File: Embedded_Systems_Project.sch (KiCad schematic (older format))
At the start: 1 part

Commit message: Deleted the Mcu
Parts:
- removed U?: ATmega2560-16AU, Package_QFP:TQFP-100_14x14mm_P0.5mm, symbol MCU_Microchip_ATmega:ATmega2560-16AU
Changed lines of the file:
@@
 Comment4 ""
 $EndDescr
-$Comp
-L MCU_Microchip_ATmega:ATmega2560-16AU U?
-U 1 1 606B9968
-P 4750 3800
-F 0 "U?" H 4750 811 50  0000 C CNN
-F 1 "ATmega2560-16AU" H 4650 3850 50  0000 C CNN
-F 2 "Package_QFP:TQFP-100_14x14mm_P0.5mm" H 4750 3800 50  0001 C CIN
-F 3 "http://ww1.microchip.com/downloads/en/DeviceDoc/Atmel-2549-8-bit-AVR-Microcontroller-ATmega640-1280-1281-2560-2561_datasheet.pdf" H 4750 3800 50  0001 C CNN
-	1    4750 3800
-	1    0    0    -1
-$EndComp
 $EndSCHEMATC

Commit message: updated component schematic
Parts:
- added U?: ATmega2560, symbol ATmega2560:ATmega2560
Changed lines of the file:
@@
 encoding utf-8
 Sheet 1 1
-Title "ESP"
+Title "Embedded Systems Projects"
 Date "2021-04-05"
 Rev "v1.0"
-Comp "studnts"
+Comp "students"
 Comment1 "firs trial"
 Comment2 ""
@@
 Comment4 ""
 $EndDescr
+$Comp
+L ATmega2560:ATmega2560 U?
+U 1 1 606C76A0
+P 5200 3750
+F 0 "U?" H 6744 3921 50  0000 L CNN
+F 1 "ATmega2560" H 6744 3830 50  0000 L CNN
+F 2 "" H 3100 6850 50  0001 C CNN
+F 3 "" H 3100 6850 50  0001 C CNN
+	1    5200 3750
+	1    0    0    -1
+$EndComp
 $EndSCHEMATC

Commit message: added footprint
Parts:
- U1: renamed from U?; footprint (none) -> Package_QFP:TQFP-100_14x14mm_P0.5mm
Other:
- moved on the sheet: U1
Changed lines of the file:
@@
 $EndDescr
 $Comp
-L ATmega2560:ATmega2560 U?
+L ATmega2560:ATmega2560 U1
 U 1 1 606C76A0
-P 5200 3750
-F 0 "U?" H 6744 3921 50  0000 L CNN
-F 1 "ATmega2560" H 6744 3830 50  0000 L CNN
-F 2 "" H 3100 6850 50  0001 C CNN
-F 3 "" H 3100 6850 50  0001 C CNN
-	1    5200 3750
+P 7800 3200
+F 0 "U1" H 9344 3371 50  0000 L CNN
+F 1 "ATmega2560" H 9344 3280 50  0000 L CNN
+F 2 "Package_QFP:TQFP-100_14x14mm_P0.5mm" H 5700 6300 50  0001 C CNN
+F 3 "https://ww1.microchip.com/downloads/en/DeviceDoc/ATmega640-1280-1281-2560-2561-Datasheet-DS40002211A.pdf" H 5700 6300 50  0001 C CNN
+	1    7800 3200
 	1    0    0    -1
 $EndComp

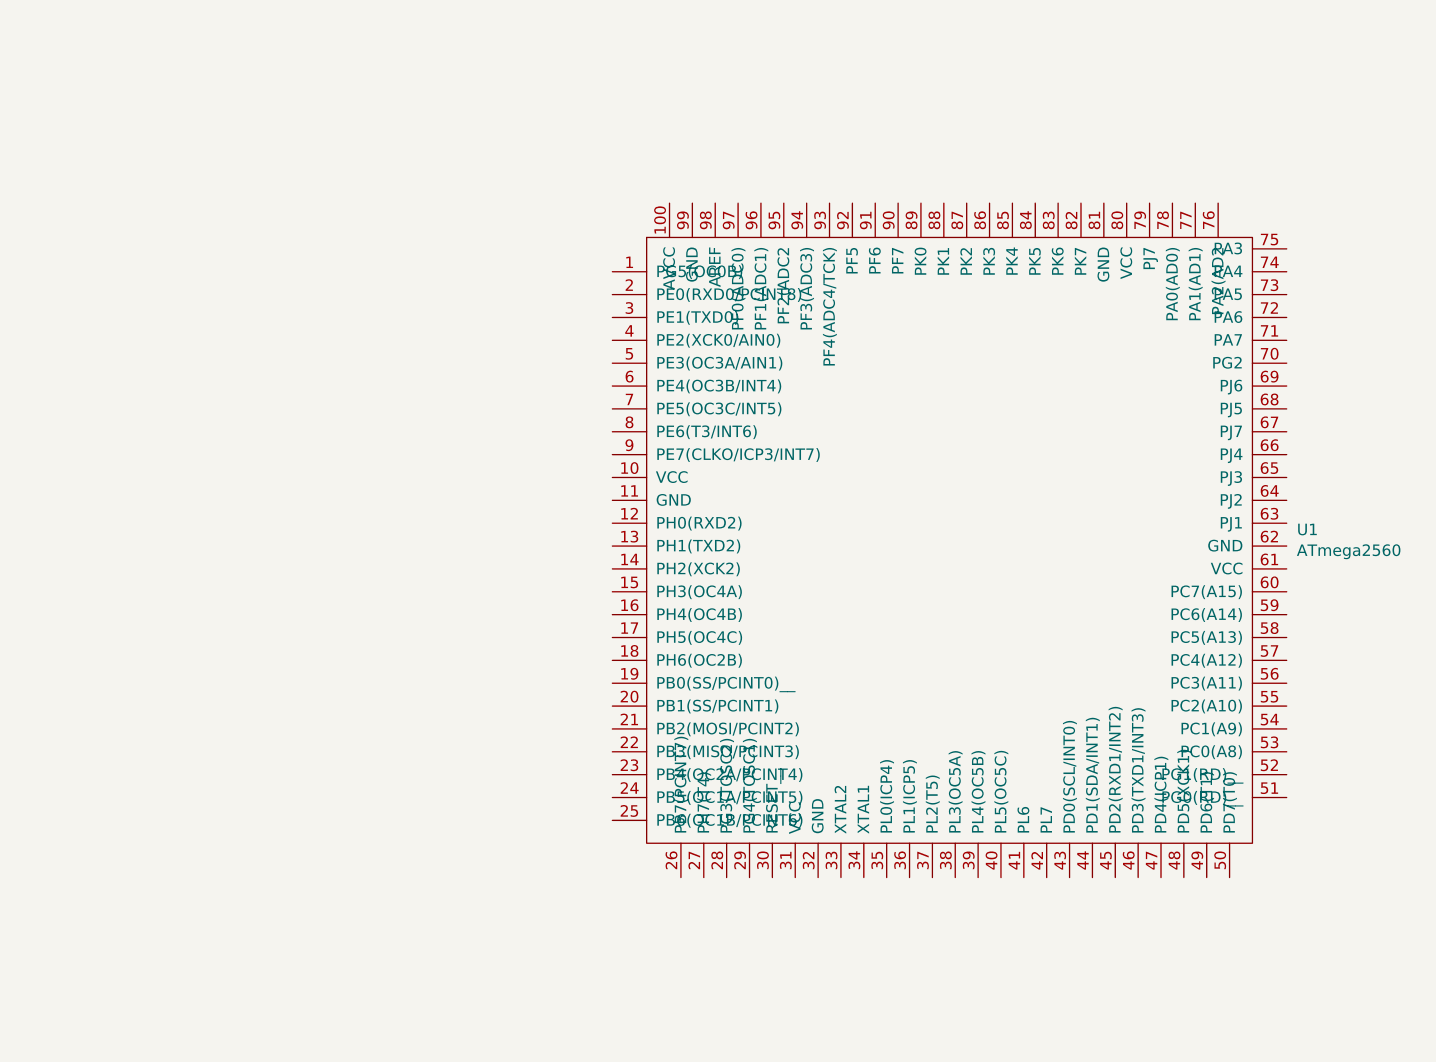
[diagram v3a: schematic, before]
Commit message: added cristal Oscillator
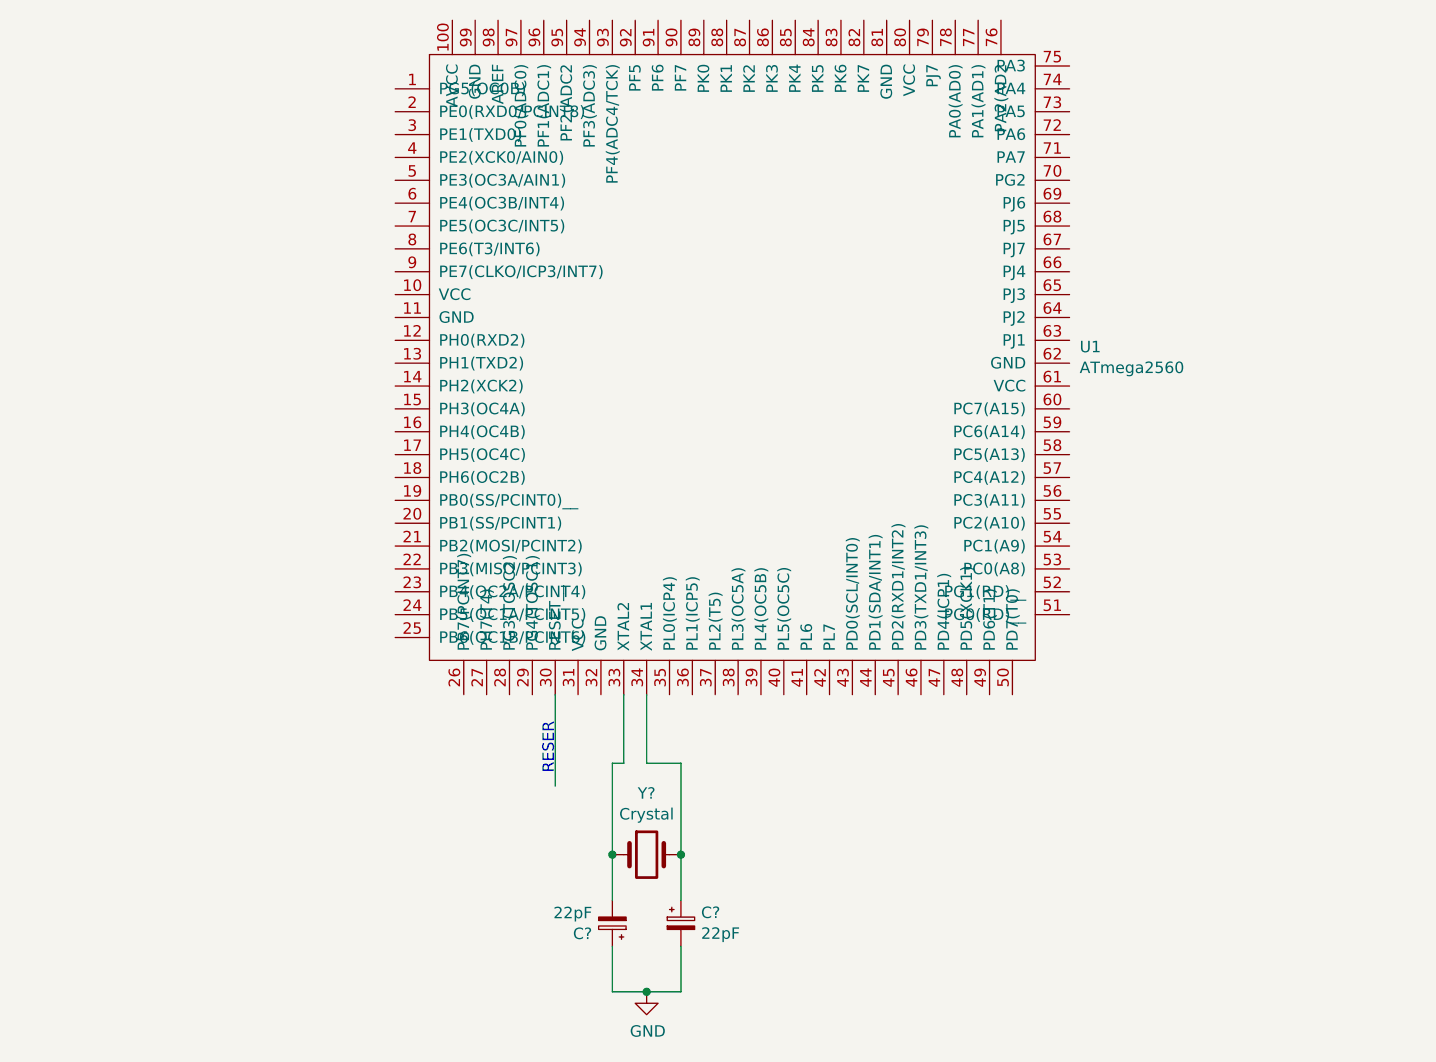
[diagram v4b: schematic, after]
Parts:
- added C? (x2): 22pF, symbol Device:CP_Small
- added Y?: Crystal, symbol Device:Crystal
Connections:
- net labels added: GND
- wire segments 0 -> 13
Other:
- note added: "RESER"
- moved on the sheet: U1
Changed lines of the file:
@@
 Comment4 ""
 $EndDescr
+Text Notes 6100 4100 1    50   ~ 0
+RESER
+Wire Wire Line
+	6100 3750 6100 4150
+$Comp
+L Device:Crystal Y?
+U 1 1 608D02D6
+P 6500 4450
+F 0 "Y?" H 6500 4718 50  0000 C CNN
+F 1 "Crystal" H 6500 4627 50  0000 C CNN
+F 2 "" H 6500 4450 50  0001 C CNN
+F 3 "~" H 6500 4450 50  0001 C CNN
+	1    6500 4450
+	1    0    0    -1
+$EndComp
 $Comp
 L ATmega2560:ATmega2560 U1
 U 1 1 606C76A0
-P 7800 3200
-F 0 "U1" H 9344 3371 50  0000 L CNN
-F 1 "ATmega2560" H 9344 3280 50  0000 L CNN
-F 2 "Package_QFP:TQFP-100_14x14mm_P0.5mm" H 5700 6300 50  0001 C CNN
-F 3 "https://ww1.microchip.com/downloads/en/DeviceDoc/ATmega640-1280-1281-2560-2561-Datasheet-DS40002211A.pdf" H 5700 6300 50  0001 C CNN
-	1    7800 3200
+P 6850 2400
+F 0 "U1" H 8394 2571 50  0000 L CNN
+F 1 "ATmega2560" H 8394 2480 50  0000 L CNN
+F 2 "Package_QFP:TQFP-100_14x14mm_P0.5mm" H 4750 5500 50  0001 C CNN
+F 3 "https://ww1.microchip.com/downloads/en/DeviceDoc/ATmega640-1280-1281-2560-2561-Datasheet-DS40002211A.pdf" H 4750 5500 50  0001 C CNN
+	1    6850 2400
 	1    0    0    -1
 $EndComp
+Wire Wire Line
+	6500 3750 6500 4050
+Wire Wire Line
+	6500 4050 6650 4050
+Wire Wire Line
+	6650 4050 6650 4450
+$Comp
+L Device:CP_Small C?
+U 1 1 608FB5B9
+P 6650 4750
+F 0 "C?" H 6738 4796 50  0000 L CNN
+F 1 "22pF" H 6738 4705 50  0000 L CNN
+F 2 "" H 6650 4750 50  0001 C CNN
+F 3 "~" H 6650 4750 50  0001 C CNN
+	1    6650 4750
+	1    0    0    -1
+$EndComp
+$Comp
+L Device:CP_Small C?
+U 1 1 608F964F
+P 6350 4750
+F 0 "C?" H 6438 4796 50  0000 L CNN
+F 1 "22pF" H 6438 4705 50  0000 L CNN
+F 2 "" H 6350 4750 50  0001 C CNN
+F 3 "~" H 6350 4750 50  0001 C CNN
+	1    6350 4750
+	-1   0    0    1
+$EndComp
+Wire Wire Line
+	6650 4450 6650 4650
+Connection ~ 6650 4450
+Wire Wire Line
+	6400 3750 6400 4050
+Wire Wire Line
+	6400 4050 6350 4050
+Wire Wire Line
+	6350 4050 6350 4450
+Wire Wire Line
+	6350 4450 6350 4650
+Connection ~ 6350 4450
+Wire Wire Line
+	6350 4850 6350 5050
+Wire Wire Line
+	6350 5050 6500 5050
+Wire Wire Line
+	6650 5050 6650 4850
+$Comp
+L power:GND #PWR?
+U 1 1 60943889
+P 6500 5050
+F 0 "#PWR?" H 6500 4800 50  0001 C CNN
+F 1 "GND" H 6505 4877 50  0000 C CNN
+F 2 "" H 6500 5050 50  0001 C CNN
+F 3 "" H 6500 5050 50  0001 C CNN
+	1    6500 5050
+	1    0    0    -1
+$EndComp
+Connection ~ 6500 5050
+Wire Wire Line
+	6500 5050 6650 5050
 $EndSCHEMATC
